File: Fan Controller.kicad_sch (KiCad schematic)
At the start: 48 parts, among them J1 Power Input, J2 4-Pin Fan Header, J3 4-Pin Fan Header, J4 I2C, J5 I2C, J6 Expansion 1, J7 Expansion 2, Q1 SQD19P06-60L_GE3, U1 ESP32-C3-SuperMini, U2 AP63205QWU-7, U3 SN74LVC2G06DBVR, U4 AP63201QWU-7

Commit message: Better buck power reliability. Better placement of some distant elements.
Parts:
- added C19: 47µF / 25V Hybrid, Capacitor_SMD:CP_Elec_6.3x5.8, symbol Device:C_Polarized_Small
- C1: value 10µF -> 47µF; footprint Capacitor_SMD:C_1206_3216Metric -> Capacitor_SMD:C_1210_3225Metric; LCSC C89632 -> C84494; MANUFACTURER Samsung Electro-Mechanics -> Murata; MPN CL31B106KBHNNNE -> GRM32ER71A476KE15L
- C8, C9: value 22µF -> 47µF; footprint Capacitor_SMD:C_1206_3216Metric -> Capacitor_SMD:C_1210_3225Metric; LCSC C710711 -> C84494; MPN GCM31CR71A226ME02L -> GRM32ER71A476KE15L
- R1, R2: value 100R -> 47R; LCSC C105577 -> C126351; MPN RC0805FR-07100RL -> RC0805FR-0747KL
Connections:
- net +12V_FAN: now also C19.1
- net GND: now also C19.2
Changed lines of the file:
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@@
 			)
 		)
-		(property "Value" "22µF"
+		(property "Value" "47µF"
 			(at 148.59 39.3762 0)
 			(show_name no)
@@
 			)
 		)
-		(property "Footprint" "Capacitor_SMD:C_1206_3216Metric"
+		(property "Footprint" "Capacitor_SMD:C_1210_3225Metric"
 			(at 146.05 38.1 0)
 			(hide yes)
@@
 			)
 		)
-		(property "Datasheet" ""
+		(property "Datasheet" "https://www.murata.com/en-eu/products/productdetail?partno=GRM32ER71A476KE15L"
 			(at 146.05 38.1 0)
 			(hide yes)
@@
 			)
 		)
-		(property "MPN" "GCM31CR71A226ME02L"
+		(property "MPN" "GRM32ER71A476KE15L"
 			(at 146.05 38.1 0)
 			(hide yes)
@@
 			)
 		)
-		(property "LCSC" "C710711"
+		(property "LCSC" "C84494"
 			(at 146.05 38.1 0)
 			(hide yes)
@@
 			)
 		)
-		(property "Value" "100R"
+		(property "Value" "47R"
 			(at 149.86 144.7799 0)
 			(show_name no)
@@
 			)
 		)
-		(property "MPN" "RC0805FR-07100RL"
+		(property "MPN" "RC0805FR-0747KL"
 			(at 147.32 143.51 0)
 			(hide yes)
@@
 			)
 		)
-		(property "LCSC" "C105577"
+		(property "LCSC" "C126351"
 			(at 147.32 143.51 0)
 			(hide yes)
@@
 			)
 		)
-		(property "Value" "100R"
+		(property "Value" "47R"
 			(at 149.86 166.3699 0)
 			(show_name no)
@@
 			)
 		)
-		(property "MPN" "RC0805FR-07100RL"
+		(property "MPN" "RC0805FR-0747KL"
 			(at 147.32 165.1 0)
 			(hide yes)
@@
 			)
 		)
-		(property "LCSC" "C105577"
+		(property "LCSC" "C126351"
 			(at 147.32 165.1 0)
 			(hide yes)
@@
 			)
 		)
-		(property "Value" "22µF"
+		(property "Value" "47µF"
 			(at 161.29 39.3762 0)
 			(show_name no)
@@
 			)
 		)
-		(property "Footprint" "Capacitor_SMD:C_1206_3216Metric"
+		(property "Footprint" "Capacitor_SMD:C_1210_3225Metric"
 			(at 158.75 38.1 0)
 			(hide yes)
@@
 			)
 		)
-		(property "Datasheet" ""
+		(property "Datasheet" "https://www.murata.com/en-eu/products/productdetail?partno=GRM32ER71A476KE15L"
 			(at 158.75 38.1 0)
 			(hide yes)
@@
 			)
 		)
-		(property "MPN" "GCM31CR71A226ME02L"
+		(property "MPN" "GRM32ER71A476KE15L"
 			(at 158.75 38.1 0)
 			(hide yes)
@@
 			)
 		)
-		(property "LCSC" "C710711"
+		(property "LCSC" "C84494"
 			(at 158.75 38.1 0)
 			(hide yes)
@@
 			)
 		)
-		(property "Value" "10µF"
+		(property "Value" "47µF"
 			(at 267.97 31.7562 0)
 			(show_name no)
@@
 			)
 		)
-		(property "Footprint" "Capacitor_SMD:C_1206_3216Metric"
+		(property "Footprint" "Capacitor_SMD:C_1210_3225Metric"
 			(at 265.43 30.48 0)
 			(hide yes)
@@
 			)
 		)
-		(property "Datasheet" ""
+		(property "Datasheet" "https://www.murata.com/en-eu/products/productdetail?partno=GRM32ER71A476KE15L"
 			(at 265.43 30.48 0)
 			(hide yes)
@@
 			)
 		)
-		(property "MPN" "CL31B106KBHNNNE"
+		(property "MPN" "GRM32ER71A476KE15L"
 			(at 265.43 30.48 0)
 			(hide yes)
@@
 			)
 		)
-		(property "MANUFACTURER" "Samsung Electro-Mechanics"
+		(property "MANUFACTURER" "Murata"
 			(at 265.43 30.48 0)
 			(hide yes)
@@
 			)
 		)
-		(property "LCSC" "C89632"
+		(property "LCSC" "C84494"
 			(at 265.43 30.48 0)
 			(hide yes)
@@
 	)
 	(embedded_fonts no)
+	(symbol
+		(lib_id "Device:C_Polarized_Small")
+		(at 294.64 236.22 0)
+		(unit 1)
+		(body_style 1)
+		(exclude_from_sim no)
+		(in_bom yes)
+		(on_board yes)
+		(in_pos_files yes)
+		(dnp no)
+		(fields_autoplaced yes)
+		(property "Reference" "C19"
+			(at 297.18 234.4038 0)
+			(show_name no)
+			(do_not_autoplace no)
+			(effects
+				(font
+					(size 1.27 1.27)
+				)
+				(justify left)
+			)
+		)
+		(property "Value" "47µF / 25V Hybrid"
+			(at 297.18 236.9438 0)
+			(show_name no)
+			(do_not_autoplace no)
+			(effects
+				(font
+					(size 1.27 1.27)
+				)
+				(justify left)
+			)
+		)
+		(property "Footprint" "Capacitor_SMD:CP_Elec_6.3x5.8"
+			(at 294.64 236.22 0)
+			(hide yes)
+			(show_name no)
+			(do_not_autoplace no)
+			(effects
+				(font
+					(size 1.27 1.27)
+				)
+			)
+		)
+		(property "Datasheet" "https://industrial.panasonic.com/ww/products/pt/hybrid-aluminum/models/EEHZC1E470P"
+			(at 294.64 236.22 0)
+			(hide yes)
+			(show_name no)
+			(do_not_autoplace no)
+			(effects
+				(font
+					(size 1.27 1.27)
+				)
+			)
+		)
+		(property "Description" "47uF 25V polymer hybrid aluminum electrolytic, 125C, polarized"
+			(at 294.64 236.22 0)
+			(hide yes)
+			(show_name no)
+			(do_not_autoplace no)
+			(effects
+				(font
+					(size 1.27 1.27)
+				)
+			)
+		)
+		(property "MPN" "EEHZC1E470P"
+			(at 294.64 236.22 0)
+			(hide yes)
+			(show_name no)
+			(do_not_autoplace no)
+			(effects
+				(font
+					(size 1.27 1.27)
+				)
+			)
+		)
+		(property "MANUFACTURER" "Panasonic"
+			(at 294.64 236.22 0)
+			(hide yes)
+			(show_name no)
+			(do_not_autoplace no)
+			(effects
+				(font
+					(size 1.27 1.27)
+				)
+			)
+		)
+		(property "LCSC" "C542308"
+			(at 294.64 236.22 0)
+			(hide yes)
+			(show_name no)
+			(do_not_autoplace no)
+			(effects
+				(font
+					(size 1.27 1.27)
+				)
+			)
+		)
+		(pin "2"
+		)
+		(pin "1"
+		)
+		(instances
+			(project "Fan Controller"
+				(path "/94c56d96-6d29-437f-bc46-cb7c0eff180b"
+					(reference "C19")
+					(unit 1)
+				)
+			)
+		)
+	)
+	(wire (pts (xy 289.56 223.52) (xy 294.64 223.52)) (stroke (width 0) (type default)))
+	(wire (pts (xy 294.64 223.52) (xy 294.64 233.68)) (stroke (width 0) (type default)))
+	(wire (pts (xy 294.64 238.76) (xy 294.64 264.16)) (stroke (width 0) (type default)))
+	(wire (pts (xy 271.78 264.16) (xy 294.64 264.16)) (stroke (width 0) (type default)))
+	(junction (at 271.78 264.16) (diameter 0) (color 0 0 0 0))
 )

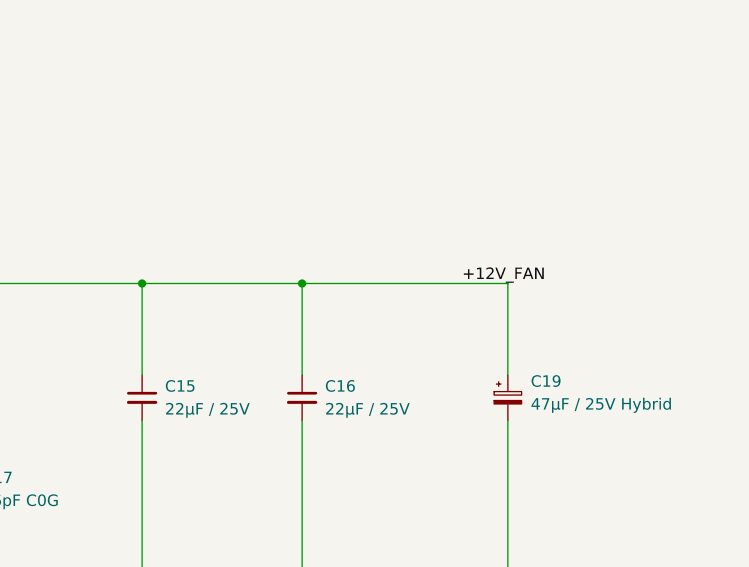
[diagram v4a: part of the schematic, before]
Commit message: R1 and 2 were 47k items added to manufacturing instead of 47R
some placement optimizations
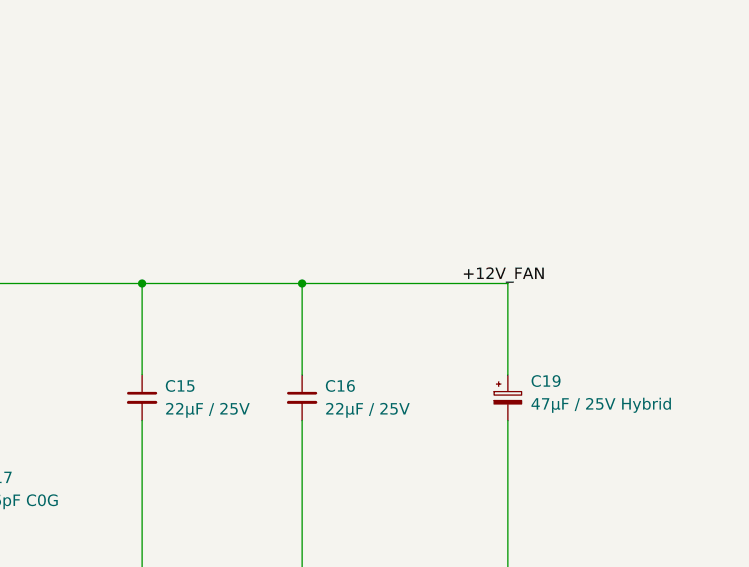
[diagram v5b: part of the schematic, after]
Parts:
- R1, R2: LCSC C126351 -> C114541; MPN RC0805FR-0747KL -> RC0805FR-0747RL
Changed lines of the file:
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@@
 	)
 	(junction
+		(at 271.78 264.16)
+		(diameter 0)
+		(color 0 0 0 0)
+	)
+	(junction
 		(at 127 115.57)
 		(diameter 0)
@@
 	(wire
 		(pts
-			(xy 271.78 223.52) (xy 289.56 223.52)
+			(xy 271.78 223.52) (xy 294.64 223.52)
 		)
 		(stroke
@@
 	(wire
 		(pts
+			(xy 294.64 223.52) (xy 294.64 233.68)
+		)
+		(stroke
+			(width 0)
+			(type default)
+		)
+	)
+	(wire
+		(pts
 			(xy 34.29 44.45) (xy 39.37 44.45)
 		)
@@
 	(wire
 		(pts
+			(xy 271.78 264.16) (xy 294.64 264.16)
+		)
+		(stroke
+			(width 0)
+			(type default)
+		)
+	)
+	(wire
+		(pts
 			(xy 252.73 124.46) (xy 261.62 124.46)
 		)
@@
 	(wire
 		(pts
+			(xy 294.64 238.76) (xy 294.64 264.16)
+		)
+		(stroke
+			(width 0)
+			(type default)
+		)
+	)
+	(wire
+		(pts
 			(xy 96.52 223.52) (xy 96.52 233.68)
 		)
@@
 	)
 	(symbol
+		(lib_id "Device:C_Polarized_Small")
+		(at 294.64 236.22 0)
+		(unit 1)
+		(body_style 1)
+		(exclude_from_sim no)
+		(in_bom yes)
+		(on_board yes)
+		(in_pos_files yes)
+		(dnp no)
+		(fields_autoplaced yes)
+		(property "Reference" "C19"
+			(at 297.18 234.4038 0)
+			(show_name no)
+			(do_not_autoplace no)
+			(effects
+				(font
+					(size 1.27 1.27)
+				)
+				(justify left)
+			)
+		)
+		(property "Value" "47µF / 25V Hybrid"
+			(at 297.18 236.9438 0)
+			(show_name no)
+			(do_not_autoplace no)
+			(effects
+				(font
+					(size 1.27 1.27)
+				)
+				(justify left)
+			)
+		)
+		(property "Footprint" "Capacitor_SMD:CP_Elec_6.3x5.8"
+			(at 294.64 236.22 0)
+			(hide yes)
+			(show_name no)
+			(do_not_autoplace no)
+			(effects
+				(font
+					(size 1.27 1.27)
+				)
+			)
+		)
+		(property "Datasheet" "https://industrial.panasonic.com/ww/products/pt/hybrid-aluminum/models/EEHZC1E470P"
+			(at 294.64 236.22 0)
+			(hide yes)
+			(show_name no)
+			(do_not_autoplace no)
+			(effects
+				(font
+					(size 1.27 1.27)
+				)
+			)
+		)
+		(property "Description" "47uF 25V polymer hybrid aluminum electrolytic, 125C, polarized"
+			(at 294.64 236.22 0)
+			(hide yes)
+			(show_name no)
+			(do_not_autoplace no)
+			(effects
+				(font
+					(size 1.27 1.27)
+				)
+			)
+		)
+		(property "MPN" "EEHZC1E470P"
+			(at 294.64 236.22 0)
+			(hide yes)
+			(show_name no)
+			(do_not_autoplace no)
+			(effects
+				(font
+					(size 1.27 1.27)
+				)
+			)
+		)
+		(property "MANUFACTURER" "Panasonic"
+			(at 294.64 236.22 0)
+			(hide yes)
+			(show_name no)
+			(do_not_autoplace no)
+			(effects
+				(font
+					(size 1.27 1.27)
+				)
+			)
+		)
+		(property "LCSC" "C542308"
+			(at 294.64 236.22 0)
+			(hide yes)
+			(show_name no)
+			(do_not_autoplace no)
+			(effects
+				(font
+					(size 1.27 1.27)
+				)
+			)
+		)
+		(pin "2"
+		)
+		(pin "1"
+		)
+		(instances
+			(project "Fan Controller"
+				(path "/94c56d96-6d29-437f-bc46-cb7c0eff180b"
+					(reference "C19")
+					(unit 1)
+				)
+			)
+		)
+	)
+	(symbol
 		(lib_id "Connector_Generic:Conn_01x05")
 		(at 266.7 119.38 0)
@@
 			)
 		)
-		(property "MPN" "RC0805FR-0747KL"
+		(property "MPN" "RC0805FR-0747RL"
 			(at 147.32 143.51 0)
 			(hide yes)
@@
 			)
 		)
-		(property "LCSC" "C126351"
+		(property "LCSC" "C114541"
 			(at 147.32 143.51 0)
 			(hide yes)
@@
 			)
 		)
-		(property "MPN" "RC0805FR-0747KL"
+		(property "MPN" "RC0805FR-0747RL"
 			(at 147.32 165.1 0)
 			(hide yes)
@@
 			)
 		)
-		(property "LCSC" "C126351"
+		(property "LCSC" "C114541"
 			(at 147.32 165.1 0)
 			(hide yes)
@@
 	)
 	(embedded_fonts no)
-	(symbol
-		(lib_id "Device:C_Polarized_Small")
-		(at 294.64 236.22 0)
-		(unit 1)
-		(body_style 1)
-		(exclude_from_sim no)
-		(in_bom yes)
-		(on_board yes)
-		(in_pos_files yes)
-		(dnp no)
-		(fields_autoplaced yes)
-		(property "Reference" "C19"
-			(at 297.18 234.4038 0)
-			(show_name no)
-			(do_not_autoplace no)
-			(effects
-				(font
-					(size 1.27 1.27)
-				)
-				(justify left)
-			)
-		)
-		(property "Value" "47µF / 25V Hybrid"
-			(at 297.18 236.9438 0)
-			(show_name no)
-			(do_not_autoplace no)
-			(effects
-				(font
-					(size 1.27 1.27)
-				)
-				(justify left)
-			)
-		)
-		(property "Footprint" "Capacitor_SMD:CP_Elec_6.3x5.8"
-			(at 294.64 236.22 0)
-			(hide yes)
-			(show_name no)
-			(do_not_autoplace no)
-			(effects
-				(font
-					(size 1.27 1.27)
-				)
-			)
-		)
-		(property "Datasheet" "https://industrial.panasonic.com/ww/products/pt/hybrid-aluminum/models/EEHZC1E470P"
-			(at 294.64 236.22 0)
-			(hide yes)
-			(show_name no)
-			(do_not_autoplace no)
-			(effects
-				(font
-					(size 1.27 1.27)
-				)
-			)
-		)
-		(property "Description" "47uF 25V polymer hybrid aluminum electrolytic, 125C, polarized"
-			(at 294.64 236.22 0)
-			(hide yes)
-			(show_name no)
-			(do_not_autoplace no)
-			(effects
-				(font
-					(size 1.27 1.27)
-				)
-			)
-		)
-		(property "MPN" "EEHZC1E470P"
-			(at 294.64 236.22 0)
-			(hide yes)
-			(show_name no)
-			(do_not_autoplace no)
-			(effects
-				(font
-					(size 1.27 1.27)
-				)
-			)
-		)
-		(property "MANUFACTURER" "Panasonic"
-			(at 294.64 236.22 0)
-			(hide yes)
-			(show_name no)
-			(do_not_autoplace no)
-			(effects
-				(font
-					(size 1.27 1.27)
-				)
-			)
-		)
-		(property "LCSC" "C542308"
-			(at 294.64 236.22 0)
-			(hide yes)
-			(show_name no)
-			(do_not_autoplace no)
-			(effects
-				(font
-					(size 1.27 1.27)
-				)
-			)
-		)
-		(pin "2"
-		)
-		(pin "1"
-		)
-		(instances
-			(project "Fan Controller"
-				(path "/94c56d96-6d29-437f-bc46-cb7c0eff180b"
-					(reference "C19")
-					(unit 1)
-				)
-			)
-		)
-	)
-	(wire (pts (xy 289.56 223.52) (xy 294.64 223.52)) (stroke (width 0) (type default)))
-	(wire (pts (xy 294.64 223.52) (xy 294.64 233.68)) (stroke (width 0) (type default)))
-	(wire (pts (xy 294.64 238.76) (xy 294.64 264.16)) (stroke (width 0) (type default)))
-	(wire (pts (xy 271.78 264.16) (xy 294.64 264.16)) (stroke (width 0) (type default)))
-	(junction (at 271.78 264.16) (diameter 0) (color 0 0 0 0))
 )

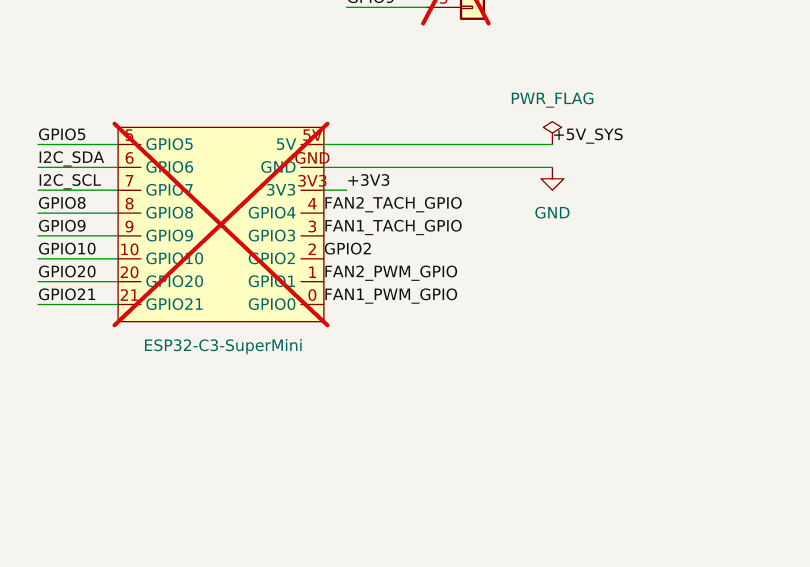
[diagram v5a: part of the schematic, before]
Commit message: Redesigned the 3V3 layout resulting in a much neater trace run. Widened the power rails
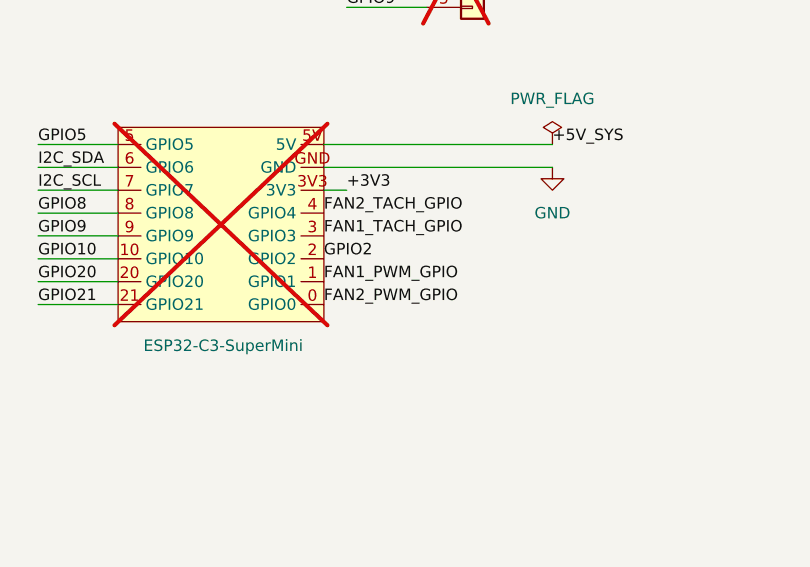
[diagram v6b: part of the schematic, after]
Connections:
- net FAN1_PWM_GPIO: now also U1.1 (GPIO1); no longer U1.0 (GPIO0)
- net FAN2_PWM_GPIO: now also U1.0 (GPIO0); no longer U1.1 (GPIO1)
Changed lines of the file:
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@@
+	)
+	(label "FAN1_PWM_GPIO"
+		(at 250.19 154.94 0)
+		(effects
+			(font
+				(size 1.27 1.27)
+			)
+			(justify left bottom)
+		)
 	)
 	(label "FAN1_PWM_GPIO"
@@
 	(label "FAN_BUCK_FB"
 		(at 180.34 251.46 0)
-		(effects
-			(font
-				(size 1.27 1.27)
-			)
-			(justify left bottom)
-		)
-	)
-	(label "FAN1_PWM_GPIO"
-		(at 250.19 157.48 0)
 		(effects
 			(font
@@
 	)
 	(label "FAN2_PWM_GPIO"
-		(at 250.19 154.94 0)
+		(at 250.19 157.48 0)
 		(effects
 			(font
